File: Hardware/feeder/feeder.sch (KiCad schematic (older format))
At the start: 17 parts, among them J1 pump, J2 power, J3 button_set, J4 button_select, J5 button_reset, J6 motor, Q1 BUZ11

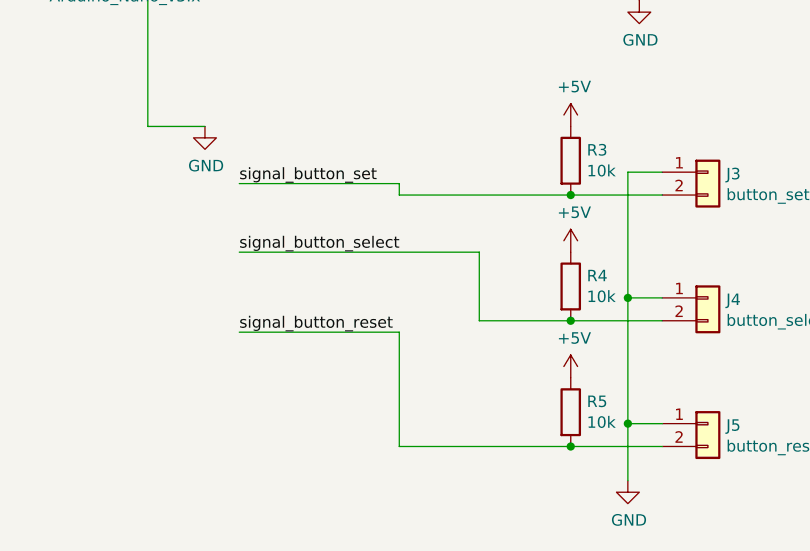
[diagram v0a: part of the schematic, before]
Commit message: More of Benno's improvements
* Increased track width to .5mm
* Added ground plane on front
* Placed multiple vias connecting both ground planes across board
* Minor schematic clean up
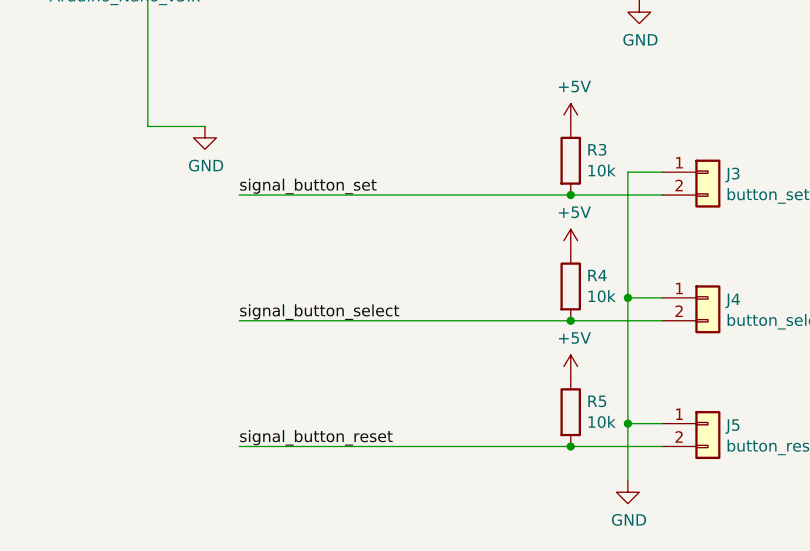
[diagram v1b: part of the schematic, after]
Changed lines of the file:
@@
 EESchema Schematic File Version 4
-EELAYER 26 0
+EELAYER 30 0
 EELAYER END
 $Descr A4 11693 8268
@@
 	1    0    0    -1
 $EndComp
-Wire Wire Line
-	2850 4400 2150 4400
-Wire Wire Line
-	2150 4050 3200 4050
-Wire Wire Line
-	2850 3750 2150 3750
-Text Label 2150 3750 0    50   ~ 0
-signal_button_set
-Text Label 2150 4050 0    50   ~ 0
+Text Label 2150 4350 0    50   ~ 0
 signal_button_select
-Text Label 2150 4400 0    50   ~ 0
+Text Label 2150 4900 0    50   ~ 0
 signal_button_reset
-Wire Wire Line
-	2850 3800 2850 3750
 Text Label 2900 1150 0    50   ~ 0
 signal_button_reset
@@
 	6750 1450 7000 1450
 Connection ~ 6750 1450
-Wire Wire Line
-	2850 3800 3600 3800
 $Comp
 L power:+5V #PWR?
@@
 Wire Wire Line
 	4000 4900 3600 4900
-Wire Wire Line
-	3600 4900 2850 4900
-Wire Wire Line
-	2850 4400 2850 4900
 Connection ~ 3600 4900
 Wire Wire Line
@@
 Wire Wire Line
 	4000 4350 3600 4350
-Wire Wire Line
-	3200 4350 3600 4350
-Wire Wire Line
-	3200 4050 3200 4350
 Connection ~ 3600 4350
 Wire Wire Line
@@
 Wire Wire Line
 	7300 1450 7300 1550
+Text Label 2150 3800 0    50   ~ 0
+signal_button_set
+Wire Wire Line
+	2150 3800 3600 3800
+Wire Wire Line
+	2150 4350 3600 4350
+Wire Wire Line
+	2150 4900 3600 4900
 $EndSCHEMATC

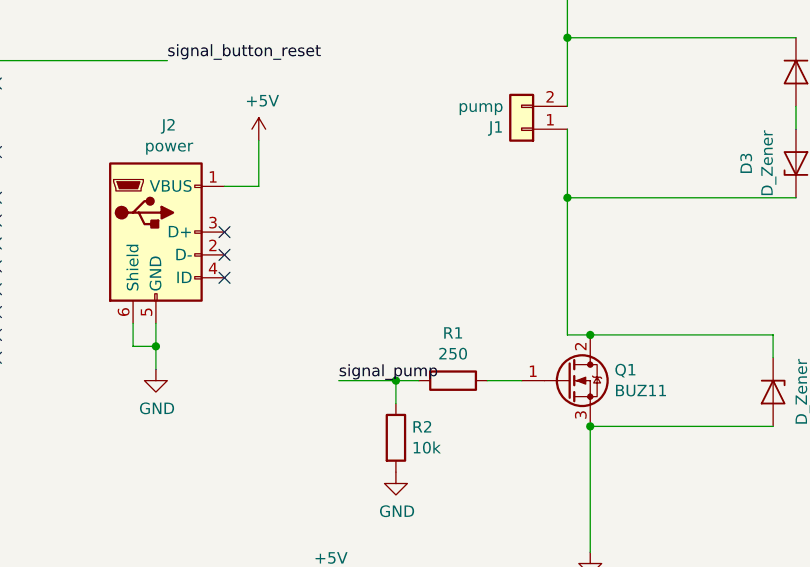
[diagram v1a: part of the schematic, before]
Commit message: Added capacitors to power supply
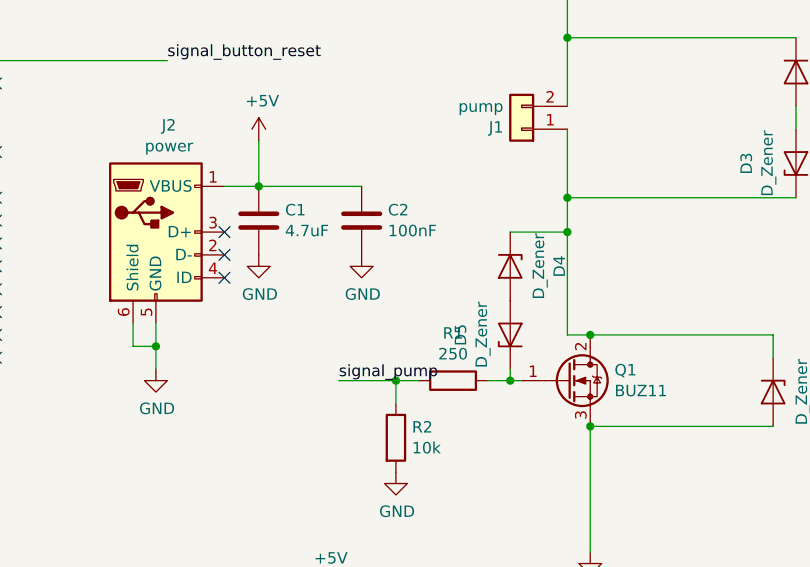
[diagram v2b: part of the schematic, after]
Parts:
- added C1: 4.7uF, Capacitor_THT:C_Rect_L7.2mm_W8.5mm_P5.00mm_FKP2_FKP2_MKS2_MKP2, symbol Device:C
- added C2: 100nF, Capacitor_THT:C_Disc_D4.3mm_W1.9mm_P5.00mm, symbol Device:C
- added D4, D5: D_Zener, Diode_THT:D_A-405_P7.62mm_Horizontal, symbol Device:D_Zener
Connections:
- net +5V: now also C1.1, C2.1
- net GND: now also C1.2, C2.2
- net at Q1.1 (G), R1.1: now also D5.1 (K)
- net at D1.1 (K), D3.1 (K), J1.1 (Pin_1)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: now also D4.1 (K)
- new net: D4.2 (A), D5.2 (A)
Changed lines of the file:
@@
 Connection ~ 4650 1750
 Wire Wire Line
-	4650 1750 4650 2350
+	4650 1750 4650 1900
 Wire Wire Line
 	4750 2350 5550 2350
@@
 Connection ~ 6750 1450
 $Comp
-L power:+5V #PWR?
+L power:+5V #PWR0107
 U 1 1 5DC05957
 P 3600 4050
-F 0 "#PWR?" H 3600 3900 50  0001 C CNN
+F 0 "#PWR0107" H 3600 3900 50  0001 C CNN
 F 1 "+5V" H 3615 4223 50  0000 C CNN
 F 2 "" H 3600 4050 50  0001 C CNN
@@
 $EndComp
 $Comp
-L power:+5V #PWR?
+L power:+5V #PWR0108
 U 1 1 5DC05984
 P 3600 4600
-F 0 "#PWR?" H 3600 4450 50  0001 C CNN
+F 0 "#PWR0108" H 3600 4450 50  0001 C CNN
 F 1 "+5V" H 3615 4773 50  0000 C CNN
 F 2 "" H 3600 4600 50  0001 C CNN
@@
 Connection ~ 3600 4350
 Wire Wire Line
-	4300 2550 4450 2550
+	4300 2550 4400 2550
 Wire Wire Line
 	4750 2750 4750 3300
 $Comp
-L power:GND #PWR?
+L power:GND #PWR0109
 U 1 1 5DC0C9C2
 P 3900 2950
-F 0 "#PWR?" H 3900 2700 50  0001 C CNN
+F 0 "#PWR0109" H 3900 2700 50  0001 C CNN
 F 1 "GND" H 3905 2777 50  0000 C CNN
 F 2 "" H 3900 2950 50  0001 C CNN
@@
 	3900 2550 3650 2550
 $Comp
-L power:GND #PWR?
+L power:GND #PWR0110
 U 1 1 5DC0E952
 P 7300 1550
-F 0 "#PWR?" H 7300 1300 50  0001 C CNN
+F 0 "#PWR0110" H 7300 1300 50  0001 C CNN
 F 1 "GND" H 7305 1377 50  0000 C CNN
 F 2 "" H 7300 1550 50  0001 C CNN
@@
 Wire Wire Line
 	2150 4900 3600 4900
+$Comp
+L Device:D_Zener D5
+U 1 1 5DC1AE71
+P 4400 2350
+F 0 "D5" H 4400 2566 50  0000 C CNN
+F 1 "D_Zener" H 4400 2475 50  0000 C CNN
+F 2 "Diode_THT:D_A-405_P7.62mm_Horizontal" H 4400 2350 50  0001 C CNN
+F 3 "~" H 4400 2350 50  0001 C CNN
+	1    4400 2350
+	0    -1   -1   0
+$EndComp
+$Comp
+L Device:D_Zener D4
+U 1 1 5DC1B2E8
+P 4400 2050
+F 0 "D4" H 4400 2266 50  0000 C CNN
+F 1 "D_Zener" H 4400 2175 50  0000 C CNN
+F 2 "Diode_THT:D_A-405_P7.62mm_Horizontal" H 4400 2050 50  0001 C CNN
+F 3 "~" H 4400 2050 50  0001 C CNN
+	1    4400 2050
+	0    1    1    0
+$EndComp
+Wire Wire Line
+	4400 2500 4400 2550
+Connection ~ 4400 2550
+Wire Wire Line
+	4400 2550 4450 2550
+Wire Wire Line
+	4400 1900 4650 1900
+Connection ~ 4650 1900
+Wire Wire Line
+	4650 1900 4650 2350
+$Comp
+L Device:C C1
+U 1 1 5DC247C1
+P 3300 1850
+F 0 "C1" H 3415 1896 50  0000 L CNN
+F 1 "4.7uF" H 3415 1805 50  0000 L CNN
+F 2 "Capacitor_THT:C_Rect_L7.2mm_W8.5mm_P5.00mm_FKP2_FKP2_MKS2_MKP2" H 3338 1700 50  0001 C CNN
+F 3 "~" H 3300 1850 50  0001 C CNN
+	1    3300 1850
+	1    0    0    -1
+$EndComp
+Connection ~ 3300 1700
+$Comp
+L Device:C C2
+U 1 1 5DC25B09
+P 3750 1850
+F 0 "C2" H 3865 1896 50  0000 L CNN
+F 1 "100nF" H 3865 1805 50  0000 L CNN
+F 2 "Capacitor_THT:C_Disc_D4.3mm_W1.9mm_P5.00mm" H 3788 1700 50  0001 C CNN
+F 3 "~" H 3750 1850 50  0001 C CNN
+	1    3750 1850
+	1    0    0    -1
+$EndComp
+$Comp
+L power:GND #PWR05
+U 1 1 5DC25E37
+P 3300 2000
+F 0 "#PWR05" H 3300 1750 50  0001 C CNN
+F 1 "GND" H 3305 1827 50  0000 C CNN
+F 2 "" H 3300 2000 50  0001 C CNN
+F 3 "" H 3300 2000 50  0001 C CNN
+	1    3300 2000
+	1    0    0    -1
+$EndComp
+$Comp
+L power:GND #PWR06
+U 1 1 5DC2613E
+P 3750 2000
+F 0 "#PWR06" H 3750 1750 50  0001 C CNN
+F 1 "GND" H 3755 1827 50  0000 C CNN
+F 2 "" H 3750 2000 50  0001 C CNN
+F 3 "" H 3750 2000 50  0001 C CNN
+	1    3750 2000
+	1    0    0    -1
+$EndComp
+Wire Wire Line
+	3300 1700 3750 1700
 $EndSCHEMATC

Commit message: Change footprints of capacitors
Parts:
- C1: footprint Capacitor_THT:C_Rect_L7.2mm_W8.5mm_P5.00mm_FKP2_FKP2_MKS2_MKP2 -> Capacitor_THT:C_Radial_D4.0mm_H5.0mm_P1.50mm
- C2: footprint Capacitor_THT:C_Disc_D4.3mm_W1.9mm_P5.00mm -> Capacitor_THT:C_Rect_L4.6mm_W3.0mm_P2.50mm_MKS02_FKP02
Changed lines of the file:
@@
 EESchema Schematic File Version 4
+LIBS:feeder-cache
 EELAYER 30 0
 EELAYER END
@@
 F 0 "C1" H 3415 1896 50  0000 L CNN
 F 1 "4.7uF" H 3415 1805 50  0000 L CNN
-F 2 "Capacitor_THT:C_Rect_L7.2mm_W8.5mm_P5.00mm_FKP2_FKP2_MKS2_MKP2" H 3338 1700 50  0001 C CNN
+F 2 "Capacitor_THT:C_Radial_D4.0mm_H5.0mm_P1.50mm" H 3338 1700 50  0001 C CNN
 F 3 "~" H 3300 1850 50  0001 C CNN
 	1    3300 1850
@@
 F 0 "C2" H 3865 1896 50  0000 L CNN
 F 1 "100nF" H 3865 1805 50  0000 L CNN
-F 2 "Capacitor_THT:C_Disc_D4.3mm_W1.9mm_P5.00mm" H 3788 1700 50  0001 C CNN
+F 2 "Capacitor_THT:C_Rect_L4.6mm_W3.0mm_P2.50mm_MKS02_FKP02" H 3788 1700 50  0001 C CNN
 F 3 "~" H 3750 1850 50  0001 C CNN
 	1    3750 1850
